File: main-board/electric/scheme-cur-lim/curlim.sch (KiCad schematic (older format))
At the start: 10 parts, among them P1 TST, P2 TST, P3 TST, Q1 bc857, Q2 irlml2244

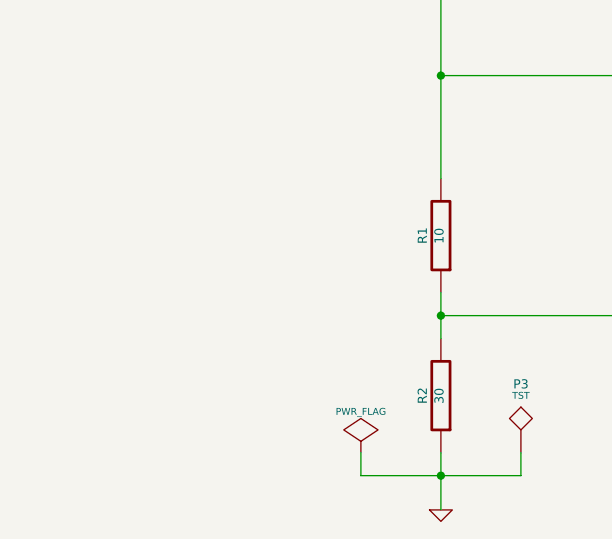
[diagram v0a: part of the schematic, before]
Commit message: Commented about upper voltage dividing resistor.
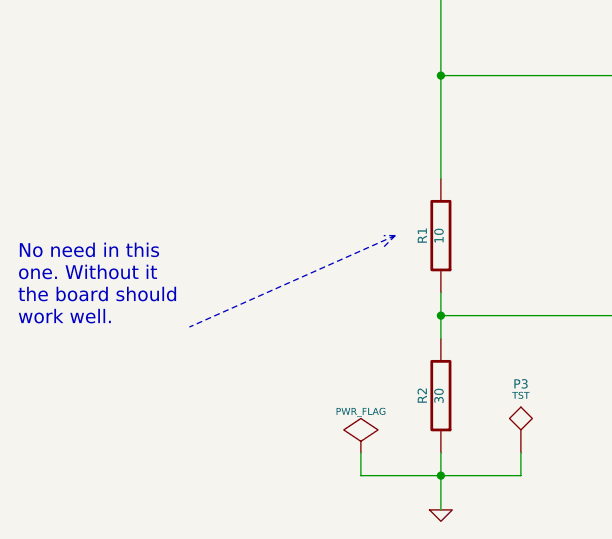
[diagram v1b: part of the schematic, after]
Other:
- note added: "No need in this \none. Without it \nthe board should \nwork well."
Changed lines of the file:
@@
 LIBS:contrib
 LIBS:valves
+LIBS:curlim-cache
 EELAYER 27 0
 EELAYER END
@@
 Sheet 1 1
 Title ""
-Date "29 oct 2013"
+Date "16 nov 2013"
 Rev ""
 Comp ""
@@
 Wire Wire Line
 	4350 4400 4350 4300
+Wire Notes Line
+	3800 3350 2900 3750
+Wire Notes Line
+	3800 3350 3750 3350
+Wire Notes Line
+	3800 3350 3750 3400
+Text Notes 2150 3750 0    60   ~ 0
+No need in this \none. Without it \nthe board should \nwork well.
 $EndSCHEMATC
